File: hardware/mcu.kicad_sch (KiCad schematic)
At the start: 38 parts, among them J1 USB-C, SW3 RUN, SW4 BOOTSEL, SW5 WP, U20 RP2350B, U21 GD25Q128ESIGR, Y1 12MHz

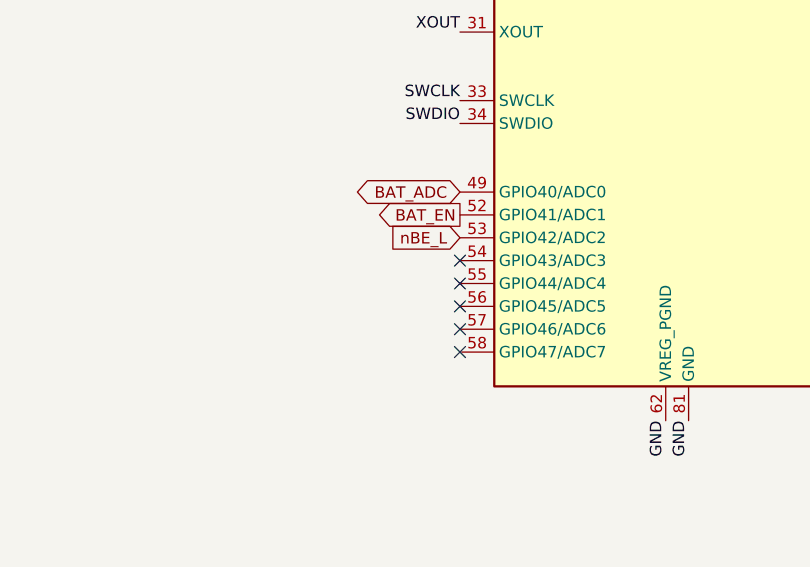
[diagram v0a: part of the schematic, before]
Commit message: Board: /INT and /NMI for the controller (open question 16)
- U7 SN74LVC2G34 brings /INT (A14) and /NMI (A15) to GPIO43/44.
- U6, a second 74LVC1G06, pulls /NMI from GPIO45 (NMI_REQ), open-drain
  like /BE; R4 holds NMI_REQ low until the firmware runs.
- Placed over fingers A14/A15 between C3 and U2. Re-routed by flow.py
  (closed on attempt 2): DRC clean, nothing unconnected; ERC has the one
  expected warning. BOMs and renders regenerated.
- Spec: pin table (46 of 48, now counting the /BE read-back), parts,
  open question 16 marked added.

Co-Authored-By: Claude Opus 5.5 <noreply@anthropic.com>
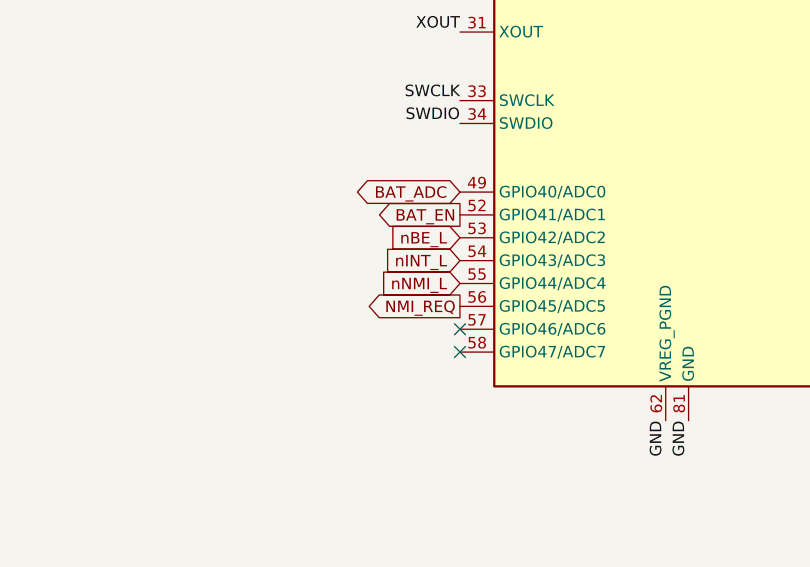
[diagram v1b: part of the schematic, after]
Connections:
- net nINT_L: now reaches U20.54 (GPIO43/ADC3)
- net nNMI_L: now reaches U20.55 (GPIO44/ADC4)
- net NMI_REQ: now reaches U20.56 (GPIO45/ADC5)
- no-connect marks 8 -> 5
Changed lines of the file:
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@@
   (global_label "BAT_EN" (shape output) (at 104.14 185.42 180) (effects (font (size 1.27 1.27)) (justify right)))
   (global_label "nBE_L" (shape input) (at 104.14 187.96 180) (effects (font (size 1.27 1.27)) (justify right)))
-  (no_connect (at 104.14 190.50))
-  (no_connect (at 104.14 193.04))
-  (no_connect (at 104.14 195.58))
+  (global_label "nINT_L" (shape input) (at 104.14 190.50 180) (effects (font (size 1.27 1.27)) (justify right)))
+  (global_label "nNMI_L" (shape input) (at 104.14 193.04 180) (effects (font (size 1.27 1.27)) (justify right)))
+  (global_label "NMI_REQ" (shape output) (at 104.14 195.58 180) (effects (font (size 1.27 1.27)) (justify right)))
   (no_connect (at 104.14 198.12))
   (no_connect (at 104.14 200.66))
